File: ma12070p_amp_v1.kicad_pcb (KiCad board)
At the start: 2 copper layers, 100.4 x 80.4 mm, 83 parts, among them U1 MAX16956AUBD/V+, U2 MA12070P

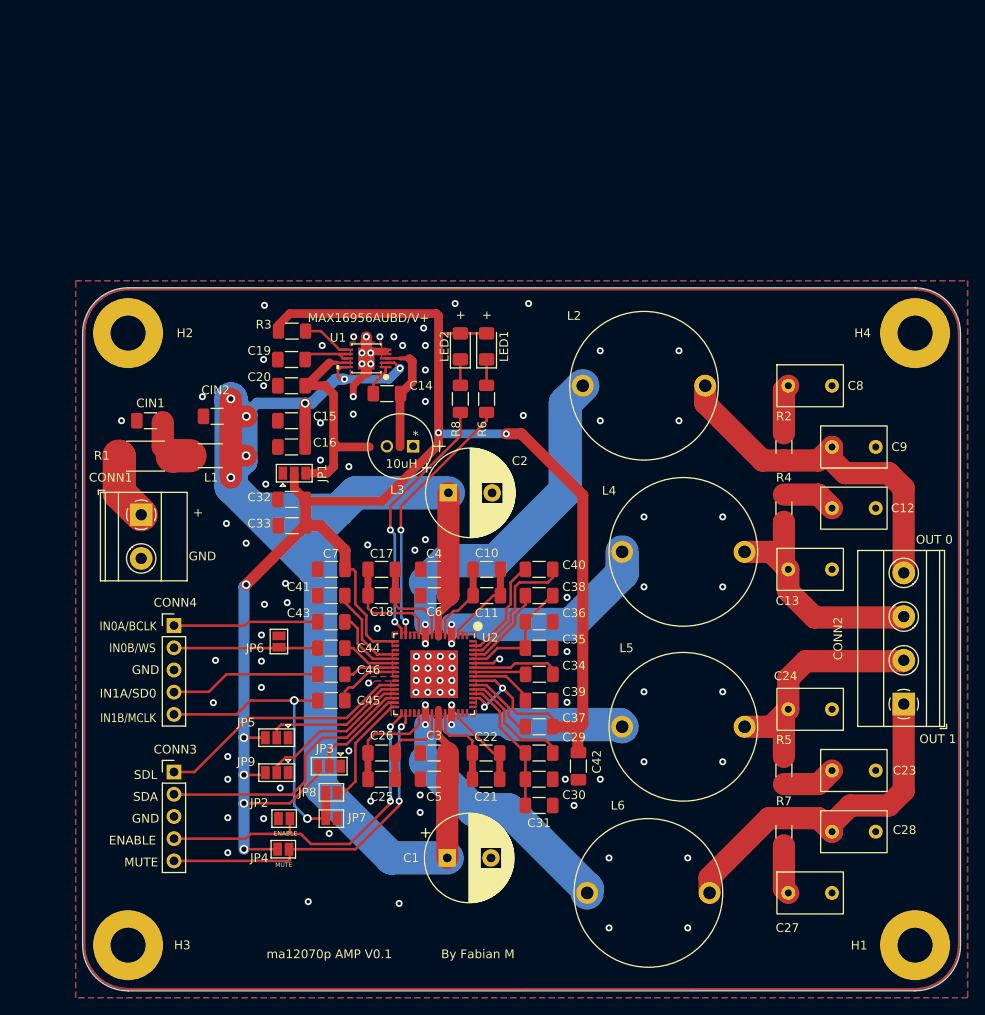
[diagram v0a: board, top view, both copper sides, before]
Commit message: layout change of power supp
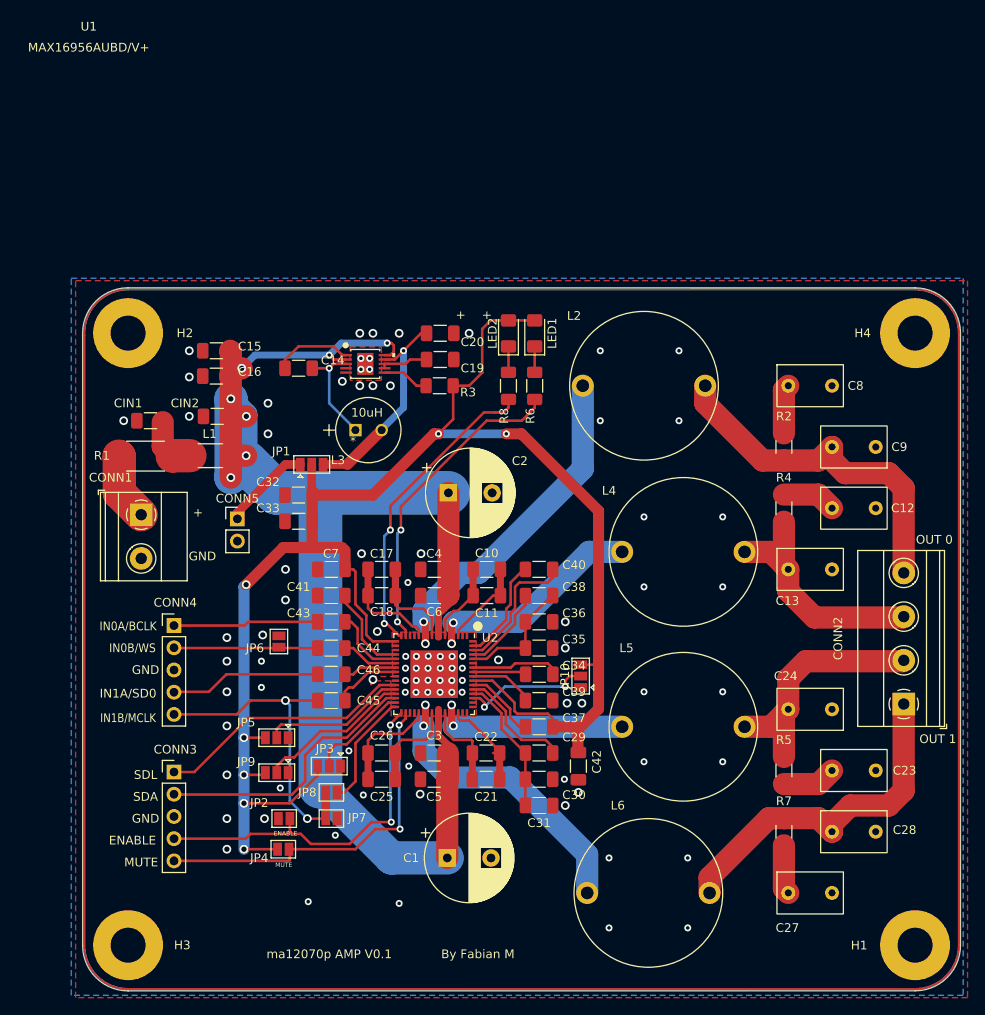
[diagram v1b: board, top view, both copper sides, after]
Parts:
- added CONN5: Conn_01x02, Connector_PinHeader_2.54mm:PinHeader_1x02_P2.54mm_Vertical, F.Cu at (127.5, 70.2)
- added JP10: SolderJumper_3_Open, Jumper:SolderJumper-3_P1.3mm_Open_Pad1.0x1.5mm, F.Cu at (166.8, 88.2)
- moved C20 18.0 mm to (150.7, 49.0), turned to 0 degrees
- moved R3 18.0 mm to (150.6, 55.0), turned to 180 degrees
- moved C19 17.0 mm to (150.7, 52.0), turned to 0 degrees
- moved C16 11.8 mm to (125.1, 53.9)
- moved C15 11.7 mm to (125.1, 51.0)
- moved C14 10.5 mm to (134.5, 53.0)
- moved LED1 5.70 mm to (161.5, 49.0)
- moved LED2 5.70 mm to (158.5, 49.0)
- moved R6 5.70 mm to (161.5, 55.0)
- moved R8 5.70 mm to (158.5, 55.0)
- moved L3 4.12 mm to (142.5, 60.0), turned to 0 degrees
- moved JP1 2.24 mm to (136.0, 64.0)
- moved C32 0.95 mm to (134.5, 67.5)
- moved C33 0.90 mm to (134.5, 70.5)
- moved U1 0.64 mm to (142.1, 52.5), turned to 0 degrees
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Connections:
- C37 pad 1: Net-(C37-Pad1) -> VDD
- C37 pad 2: VDD -> Net-(C37-Pad2)
- L1 pad 1: PVDD -> Net-(CIN1-Pad2)
- L1 pad 2: Net-(CIN1-Pad2) -> PVDD
- U2 pad 51: VDD -> MSEL0
- U2 pad 54: Net-(C37-Pad1) -> Net-(C37-Pad2)
- U2 pad 65: (no net) -> GND
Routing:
- net PVDD: track 203.2 -> 184.4 mm
- net GND: track 16.2 -> 0.25 mm, vias 95 -> 92
- net MSEL0: track 0.00 -> 14.9 mm, vias 0 -> 2
- net VDD: track 214.7 -> 203.9 mm, vias 9 -> 7
- net Ext_supply_5V: track 0.00 -> 10.2 mm
- net OUT0B: track 47.2 -> 38.3 mm
- net Net-(C37-Pad1): track 8.56 -> 0.00 mm
- net OUT1A: track 30.3 -> 21.8 mm
- net OUT0A: track 31.8 -> 25.1 mm
- net CLIP: track 29.8 -> 36.2 mm
- net ERR: track 29.3 -> 35.3 mm
- net Net-(C14-Pad1): track 3.61 -> 8.99 mm
- net OUT1B: track 38.0 -> 33.4 mm
- net Net-(C14-Pad2): track 15.5 -> 12.4 mm, vias 0 -> 1
- net MUTE: track 40.0 -> 41.7 mm
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
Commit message: return current improvements
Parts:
- moved C32 19.2 mm to (150.4, 56.8)
- moved C33 19.2 mm to (150.4, 59.8)
- moved JP1 8.69 mm to (144.0, 60.6)
- moved L3 6.20 mm to (136.5, 58.5)
- moved JP2 3.50 mm to (132.8, 108.0)
- moved JP4 3.40 mm to (132.8, 111.4)
- moved JP3 1.97 mm to (139.0, 100.2)
- moved JP7 1.91 mm to (138.4, 106.4)
- moved JP8 1.71 mm to (138.4, 103.2)
- moved CONN5 1.70 mm to (126.4, 68.9)
- moved JP5 1.35 mm to (132.0, 96.6)
- moved C45 1.25 mm to (138.2, 89.8)
- moved C19 1.20 mm to (150.7, 50.8)
- moved C20 1.20 mm to (150.7, 47.8)
- moved R3 1.20 mm to (150.6, 53.8)
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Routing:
- net VDD: track 203.9 -> 216.7 mm
- net Ext_supply_5V: track 10.2 -> 21.1 mm
- net MUTE: track 41.7 -> 31.2 mm
- net ENABLE: track 41.3 -> 32.3 mm
- net ERR: track 35.3 -> 44.0 mm
- net Net-(C37-Pad2): track 0.00 -> 8.56 mm
- net CLIP: track 36.2 -> 42.0 mm
- net AD1: track 17.7 -> 22.9 mm
- net OUT0B: track 38.3 -> 41.5 mm
- net Net-(C45-Pad1): track 36.7 -> 39.9 mm
- net SDA: track 31.6 -> 33.8 mm
- net CLKIO: track 13.3 -> 15.2 mm
- net Net-(C25-Pad2): track 12.0 -> 10.3 mm
- net AD0: track 16.4 -> 17.8 mm
- net Net-(C14-Pad1): track 8.99 -> 7.64 mm
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
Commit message: schematic optimizing
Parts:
- moved JP6 0.79 mm to (131.8, 83.6)
- moved C45 0.07 mm to (138.2, 89.7)
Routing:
- net PVDD: track 184.3 -> 157.3 mm, vias 7 -> 11
- net MUTE: track 31.2 -> 47.0 mm
- net ENABLE: track 32.3 -> 43.9 mm
- net OUT1A: track 21.8 -> 25.0 mm, vias 2 -> 3
- net OUT0A: track 25.1 -> 28.3 mm, vias 2 -> 3
- net OUT0B: track 41.5 -> 44.4 mm, vias 2 -> 3
- net OUT1B: track 33.4 -> 35.3 mm, vias 2 -> 3
- net Net-(C45-Pad1): track 39.9 -> 41.3 mm
- net AD1: track 22.9 -> 21.7 mm
- net SDA: track 33.8 -> 32.7 mm
- net IC_5V: track 25.3 -> 24.3 mm
- net CLIP: track 42.0 -> 42.8 mm
- net VDD: track 216.7 -> 215.8 mm
- net Net-(C17-Pad2): track 11.9 -> 11.1 mm
- net ERR: track 44.0 -> 44.8 mm
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- added copper zone on F.Cu, net OUT0A
- added copper zone on F.Cu, net OUT0B
- added copper zone on F.Cu, net OUT1A
- added copper zone on F.Cu, net OUT1B
- added copper zone on B.Cu, net PVDD

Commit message: minor improvements on the pcb
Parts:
- moved C4 3.00 mm to (150.1, 79.0)
- moved C6 3.00 mm to (150.1, 76.0)
- moved C5 3.00 mm to (150.6, 97.0)
- moved C3 3.00 mm to (150.6, 100.0)
- moved C14 1.64 mm to (136.0, 51.3), turned to -90 degrees
- moved C43 1.10 mm to (138.2, 82.6)
- moved C46 1.10 mm to (138.2, 88.1)
- moved C44 1.10 mm to (138.2, 85.3)
- moved C45 1.10 mm to (138.2, 90.8)
- moved JP6 1.00 mm to (131.8, 84.6)
- moved C41 0.15 mm to (138.2, 78.9)
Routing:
- net GND: track 0.61 -> 5.91 mm, vias 134 -> 214
- net Net-(C14-Pad1): track 7.64 -> 4.64 mm
- net MUTE: track 47.0 -> 44.5 mm
- net Net-(C45-Pad1): track 41.3 -> 39.7 mm
- net VDD: track 215.8 -> 214.3 mm
- net Net-(C19-Pad1): track 5.71 -> 6.89 mm
- net Net-(C43-Pad1): track 17.3 -> 16.5 mm
- net ENABLE: track 43.9 -> 44.8 mm
- net ERR: track 44.8 -> 44.0 mm
- net IN0A: track 8.01 -> 7.30 mm
- net OUT1A: track 25.0 -> 24.3 mm, vias 3 -> 4
- net OUT0A: track 28.3 -> 27.6 mm, vias 3 -> 4
- net Net-(C21-Pad1): track 9.37 -> 10.0 mm
- net Net-(C17-Pad1): track 10.6 -> 11.2 mm
- net PVDD: track 157.3 -> 156.8 mm, vias 11 -> 10
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- added copper zone on B.Cu, net OUT0A
- added copper zone on B.Cu, net OUT0B
- added copper zone on B.Cu, net OUT1A
- added copper zone on B.Cu, net OUT1B
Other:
- board text added: "ma12070p AMP V0.5 by Fabian M GPL-3.0 License"
- board text removed: "By Fabian M"
- board text removed: "ma12070p AMP V0.1"
